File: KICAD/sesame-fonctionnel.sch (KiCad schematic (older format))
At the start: 9 parts, among them J1 CXS70-14-C, J2 CXS70-14-C, J3 6095, J4 6095, J5 6095, J6 6095, J7 CXS70-14-C, J8 CXS70-14-C

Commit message: route + work on djd
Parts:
- added H1, H2, H3, H4: MountingHole, MountingHole:MountingHole_3.2mm_M3, symbol Mechanical:MountingHole
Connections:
- net LEFT PROTECTION/IO_PWR renamed L
- net RIGHT PROTECTION/IO_PWR renamed R
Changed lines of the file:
@@
 F6 "Dir" O R 1600 5300 50
 F7 "Mode" O R 1600 5400 50
-F8 "PWM" O R 1600 4100 50
-F9 "~PWM" O R 1600 4000 50
-F10 "CC_CV_Mode" O R 1600 5500 50
-F11 "Ext_Setpoint" O R 1600 6550 50
-F12 "Ext_Current_Tresh" O R 1600 7100 50
-F13 "Ext_Voltage_Tresh" O R 1600 7000 50
-F14 "Ext_Rearm" O R 1600 6850 50
-F15 "INT_PWM_Power" I R 1600 4900 50
-F16 "~INT_PWM_Freewheel" I R 1600 4800 50
+F8 "CC_CV_Mode" O R 1600 5500 50
+F9 "Ext_Setpoint" O R 1600 6550 50
+F10 "Ext_Current_Tresh" O R 1600 7100 50
+F11 "Ext_Voltage_Tresh" O R 1600 7000 50
+F12 "Ext_Rearm" O R 1600 6850 50
+F13 "INT_PWM_Power" I R 1600 4900 50
+F14 "~INT_PWM_Freewheel" I R 1600 4800 50
+F15 "PWM_Power" O R 1600 4100 50
+F16 "~PWM_Freewheel" O R 1600 4000 50
 $EndSheet
 Wire Wire Line
@@
 F5 "PWM_Power" O R 6300 5300 50
 $EndSheet
+$Comp
+L Mechanical:MountingHole H1
+U 1 1 61346C8D
+P 10450 650
+F 0 "H1" H 10550 696 50  0000 L CNN
+F 1 "MountingHole" H 10550 605 50  0000 L CNN
+F 2 "MountingHole:MountingHole_3.2mm_M3" H 10450 650 50  0001 C CNN
+F 3 "~" H 10450 650 50  0001 C CNN
+	1    10450 650
+	1    0    0    -1
+$EndComp
+$Comp
+L Mechanical:MountingHole H2
+U 1 1 613479B3
+P 10450 850
+F 0 "H2" H 10550 896 50  0000 L CNN
+F 1 "MountingHole" H 10550 805 50  0000 L CNN
+F 2 "MountingHole:MountingHole_3.2mm_M3" H 10450 850 50  0001 C CNN
+F 3 "~" H 10450 850 50  0001 C CNN
+	1    10450 850
+	1    0    0    -1
+$EndComp
+$Comp
+L Mechanical:MountingHole H3
+U 1 1 6134C741
+P 10450 1050
+F 0 "H3" H 10550 1096 50  0000 L CNN
+F 1 "MountingHole" H 10550 1005 50  0000 L CNN
+F 2 "MountingHole:MountingHole_3.2mm_M3" H 10450 1050 50  0001 C CNN
+F 3 "~" H 10450 1050 50  0001 C CNN
+	1    10450 1050
+	1    0    0    -1
+$EndComp
+$Comp
+L Mechanical:MountingHole H4
+U 1 1 613513EA
+P 10450 1250
+F 0 "H4" H 10550 1296 50  0000 L CNN
+F 1 "MountingHole" H 10550 1205 50  0000 L CNN
+F 2 "MountingHole:MountingHole_3.2mm_M3" H 10450 1250 50  0001 C CNN
+F 3 "~" H 10450 1250 50  0001 C CNN
+	1    10450 1250
+	1    0    0    -1
+$EndComp
+Text Label 1050 2200 0    50   ~ 0
+L
+Text Label 10600 2200 0    50   ~ 0
+R
 $EndSCHEMATC

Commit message: added footprint for sepic coil + no more errors in netlist
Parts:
- removed J3, J4, J5, J6: 6095, symbol Mechanical:MountingHole_Pad
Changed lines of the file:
@@
 	1000 3250 950  3250
 $Comp
-L Mechanical:MountingHole_Pad J4
+L Mechanical:MountingHole_Pad #J4
 U 1 1 6142C008
 P 800 3100
-F 0 "J4" V 1050 3150 50  0000 C CNN
+F 0 "#J4" V 1050 3150 50  0000 C CNN
 F 1 "6095" V 950 3150 50  0000 C CNN
 F 2 "" H 800 3100 50  0001 C CNN
@@
 $EndComp
 $Comp
-L Mechanical:MountingHole_Pad J3
+L Mechanical:MountingHole_Pad #J3
 U 1 1 6142711F
 P 800 2350
-F 0 "J3" V 550 2400 50  0000 C CNN
+F 0 "#J3" V 550 2400 50  0000 C CNN
 F 1 "6095" V 650 2400 50  0000 C CNN
 F 2 "" H 800 2350 50  0001 C CNN
@@
 $EndSheet
 $Comp
-L Mechanical:MountingHole_Pad J5
+L Mechanical:MountingHole_Pad #J5
 U 1 1 61485222
 P 10900 2350
-F 0 "J5" V 10650 2400 50  0000 C CNN
+F 0 "#J5" V 10650 2400 50  0000 C CNN
 F 1 "6095" V 10750 2400 50  0000 C CNN
 F 2 "" H 10900 2350 50  0001 C CNN
@@
 	10800 3050 10700 3050
 $Comp
-L Mechanical:MountingHole_Pad J6
+L Mechanical:MountingHole_Pad #J6
 U 1 1 6156FADE
 P 10900 3050
-F 0 "J6" V 11150 3100 50  0000 C CNN
+F 0 "#J6" V 11150 3100 50  0000 C CNN
 F 1 "6095" V 11050 3100 50  0000 C CNN
 F 2 "" H 10900 3050 50  0001 C CNN

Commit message: changed monting holes + tweaks & still routing
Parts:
- H1, H2, H3, H4: footprint MountingHole:MountingHole_3.2mm_M3 -> Sesame_footprint:MountingHole_3.2mm_M3
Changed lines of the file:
@@
 F 0 "H1" H 10550 696 50  0000 L CNN
 F 1 "MountingHole" H 10550 605 50  0000 L CNN
-F 2 "MountingHole:MountingHole_3.2mm_M3" H 10450 650 50  0001 C CNN
+F 2 "Sesame_footprint:MountingHole_3.2mm_M3" H 10450 650 50  0001 C CNN
 F 3 "~" H 10450 650 50  0001 C CNN
 	1    10450 650
@@
 F 0 "H2" H 10550 896 50  0000 L CNN
 F 1 "MountingHole" H 10550 805 50  0000 L CNN
-F 2 "MountingHole:MountingHole_3.2mm_M3" H 10450 850 50  0001 C CNN
+F 2 "Sesame_footprint:MountingHole_3.2mm_M3" H 10450 850 50  0001 C CNN
 F 3 "~" H 10450 850 50  0001 C CNN
 	1    10450 850
@@
 F 0 "H3" H 10550 1096 50  0000 L CNN
 F 1 "MountingHole" H 10550 1005 50  0000 L CNN
-F 2 "MountingHole:MountingHole_3.2mm_M3" H 10450 1050 50  0001 C CNN
+F 2 "Sesame_footprint:MountingHole_3.2mm_M3" H 10450 1050 50  0001 C CNN
 F 3 "~" H 10450 1050 50  0001 C CNN
 	1    10450 1050
@@
 F 0 "H4" H 10550 1296 50  0000 L CNN
 F 1 "MountingHole" H 10550 1205 50  0000 L CNN
-F 2 "MountingHole:MountingHole_3.2mm_M3" H 10450 1250 50  0001 C CNN
+F 2 "Sesame_footprint:MountingHole_3.2mm_M3" H 10450 1250 50  0001 C CNN
 F 3 "~" H 10450 1250 50  0001 C CNN
 	1    10450 1250

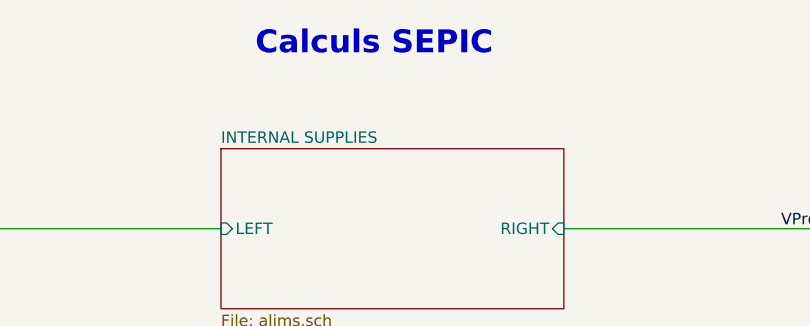
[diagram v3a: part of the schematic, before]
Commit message: mod. ref rail on kicad
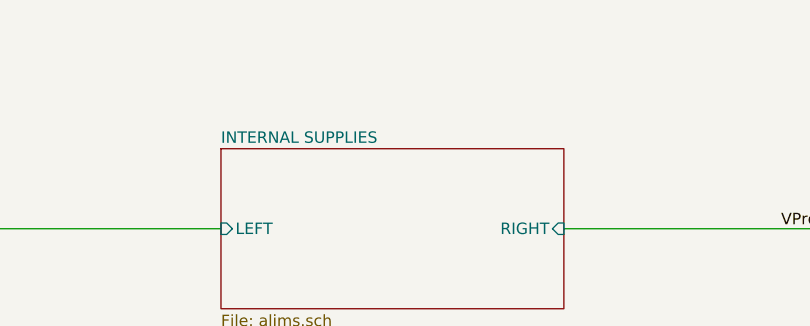
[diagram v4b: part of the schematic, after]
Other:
- note removed: "Calculs SEPIC"
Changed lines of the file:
@@
 Text Label 1950 4100 2    50   ~ 0
 PWM
-Text Notes 5200 300  0    100  ~ 20
-Calculs SEPIC
 $Sheet
 S 5050 700  1500 700

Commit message: cleanup silkscreen
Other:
- note removed: "<- VOIR PROBLEME DC"
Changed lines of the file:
@@
 Sheet 1 17
 Title "SESAME"
-Date "2021-08-17"
-Rev "0.8"
+Date "2021-08-31"
+Rev "0.9"
 Comp "ALEEA"
 Comment1 "Dessin : Guillaume Arthaud"
@@
 Voltage_Sens_L
 $Sheet
-S 3800 3200 850  550
+S 3600 3200 1050 550
 U 60F19D6C
 F0 "MOS DRIVER L" 50
 F1 "Mos_Drivers.sch" 50
 F2 "VG_P" O R 4650 3500 50
-F3 "Driver_S" I L 3800 3550 50
-F4 "Driver_P" I L 3800 3650 50
+F3 "Driver_S" I L 3600 3550 50
+F4 "Driver_P" I L 3600 3650 50
 F5 "VG_S" O R 4650 3300 50
 F6 "VS" U R 4650 3400 50
-$EndSheet
-Wire Wire Line
-	6850 2600 6850 4250
-Wire Wire Line
-	6750 4150 6750 2700
+F7 "VS_Opposite" U R 4650 3650 50
+$EndSheet
 Wire Wire Line
 	7050 1700 7050 5850
@@
 Wire Wire Line
 	2500 2200 2650 2200
-Wire Wire Line
-	4750 3300 4650 3300
-Wire Wire Line
-	4650 3400 4850 3400
-Wire Wire Line
-	4950 3500 4650 3500
-Wire Wire Line
-	6650 2800 6650 4050
-$Sheet
-S 3800 3950 850  550
+$Sheet
+S 3600 3950 1050 550
 U 619A00BB
 F0 "MOS DRIVER R" 50
 F1 "Mos_Drivers.sch" 50
-F2 "VG_P" O R 4650 4250 50
-F3 "Driver_S" I L 3800 4050 50
-F4 "Driver_P" I L 3800 4150 50
-F5 "VG_S" O R 4650 4050 50
-F6 "VS" U R 4650 4150 50
-$EndSheet
-Wire Wire Line
-	3450 3650 3800 3650
-Wire Wire Line
-	3800 3550 3450 3550
-Wire Wire Line
-	3450 4050 3800 4050
-Wire Wire Line
-	3800 4150 3450 4150
-Wire Wire Line
-	4650 4050 6650 4050
-Wire Wire Line
-	4650 4150 6750 4150
+F2 "VG_P" O R 4650 4400 50
+F3 "Driver_S" I L 3600 4050 50
+F4 "Driver_P" I L 3600 4150 50
+F5 "VG_S" O R 4650 4200 50
+F6 "VS" U R 4650 4300 50
+F7 "VS_Opposite" U R 4650 4050 50
+$EndSheet
+Wire Wire Line
+	3450 3650 3600 3650
+Wire Wire Line
+	3600 3550 3450 3550
+Wire Wire Line
+	3450 4050 3600 4050
+Wire Wire Line
+	3600 4150 3450 4150
 $Sheet
 S 5050 1950 1500 950
@@
 F9 "VS_R" U R 6550 2700 50
 $EndSheet
-Wire Wire Line
-	4650 4250 6850 4250
 $Comp
 L power:PWR_FLAG #FLG01
@@
 	1    0    0    -1
 $EndComp
-Text Notes 4800 3550 0    100  ~ 20
-<- VOIR PROBLEME DC
 $Sheet
 S 4800 5100 1500 1000
@@
 Text Label 10600 2200 0    50   ~ 0
 R
+Wire Wire Line
+	4750 3300 4650 3300
+Wire Wire Line
+	4650 3400 4850 3400
+Wire Wire Line
+	4950 3500 4650 3500
+Wire Wire Line
+	4650 4400 6850 4400
+Wire Wire Line
+	6850 2600 6850 4400
+Wire Wire Line
+	6750 4300 4650 4300
+Wire Wire Line
+	6750 2700 6750 3650
+Wire Wire Line
+	4650 4200 6650 4200
+Wire Wire Line
+	6650 2800 6650 4200
+Wire Wire Line
+	4650 3650 6750 3650
+Connection ~ 6750 3650
+Wire Wire Line
+	6750 3650 6750 4300
+Connection ~ 4850 3400
+Wire Wire Line
+	4650 4050 4850 4050
+Wire Wire Line
+	4850 4050 4850 3400
 $EndSCHEMATC

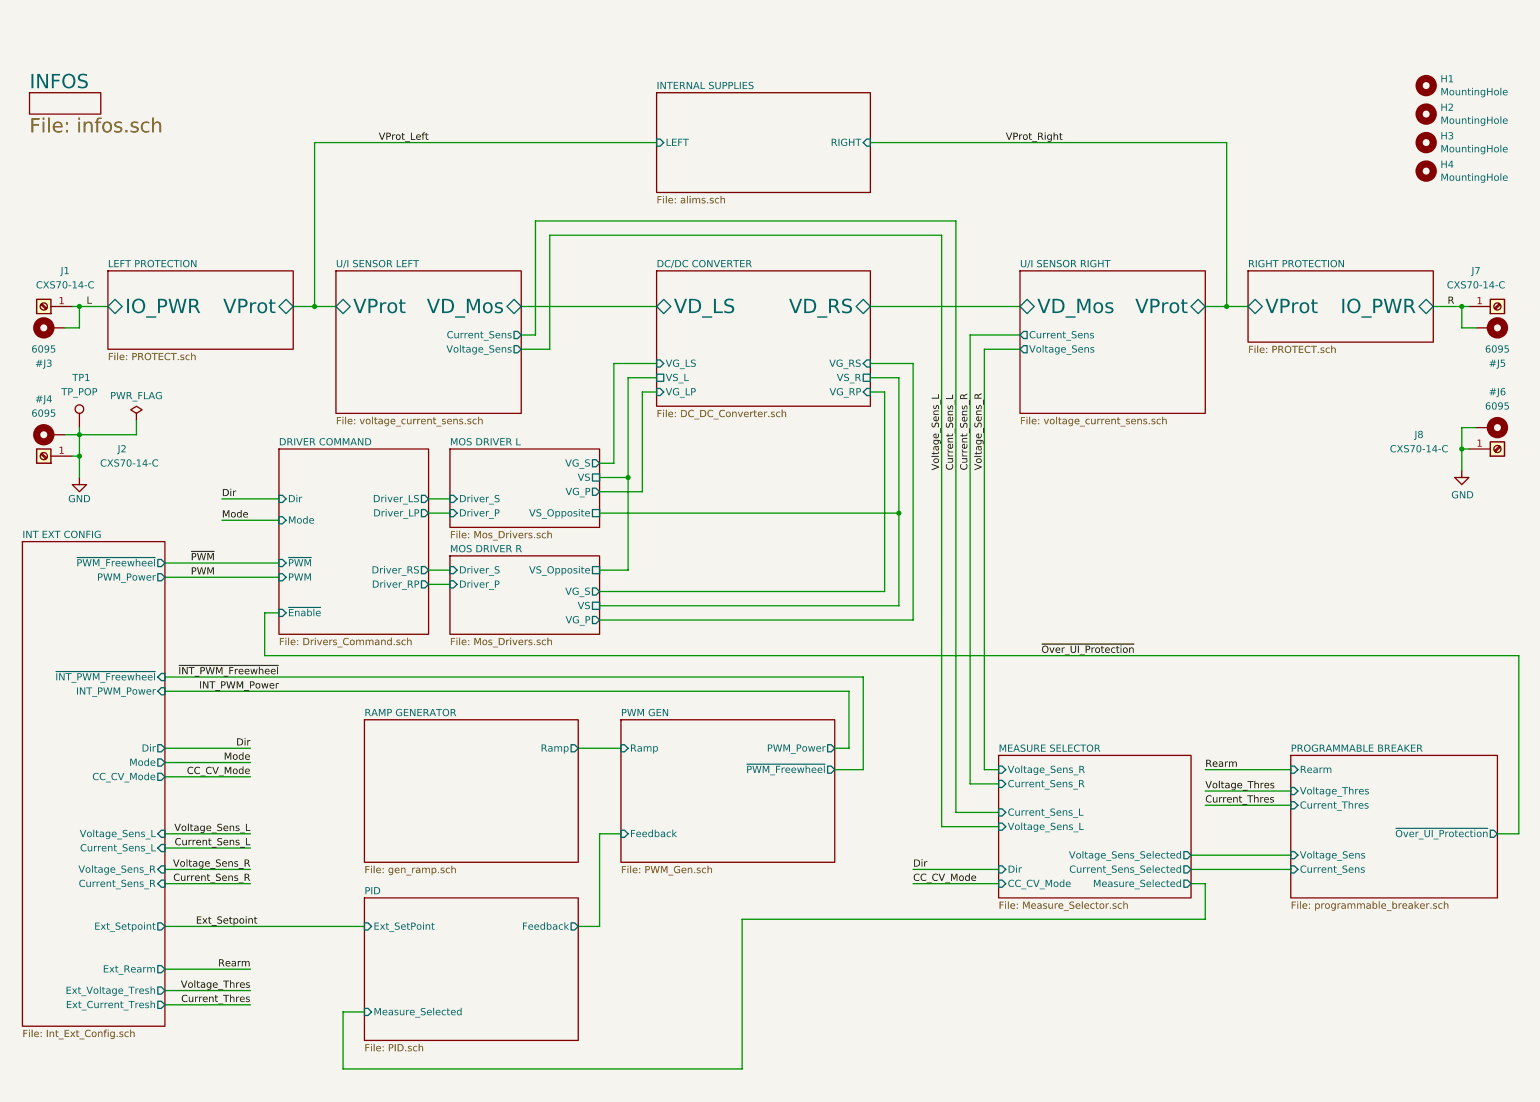
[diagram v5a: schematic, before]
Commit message: modified deadtime + added config pads on the bottom for charge pump config
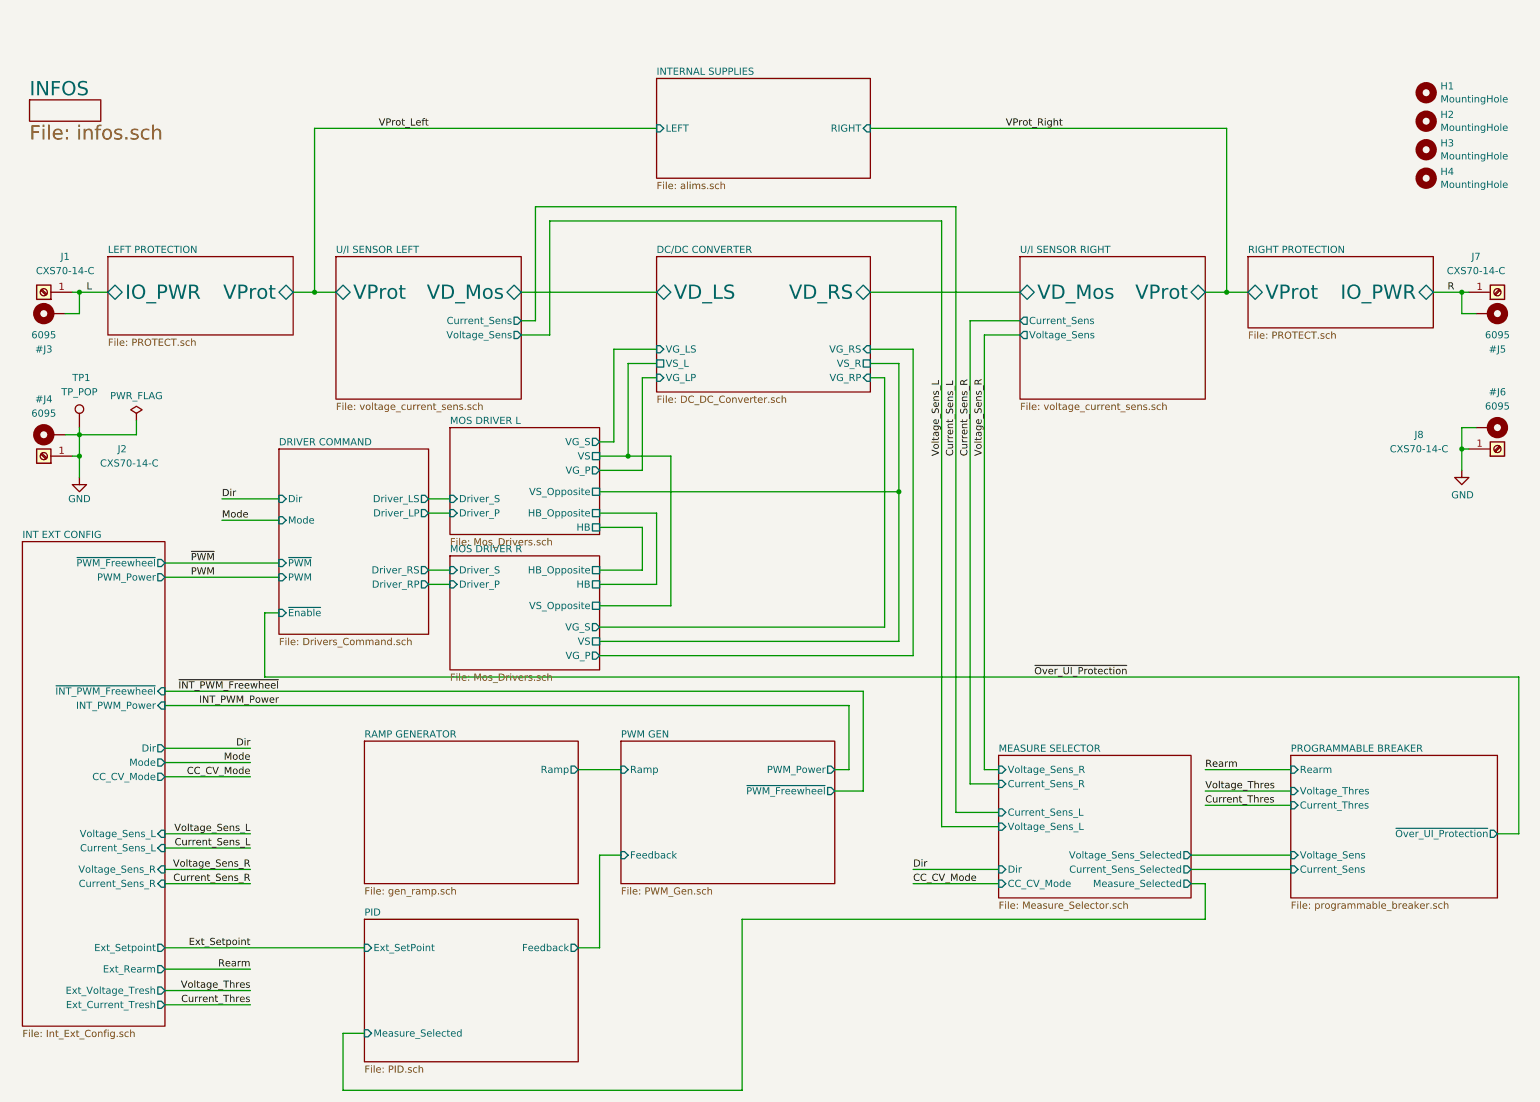
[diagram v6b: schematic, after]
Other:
- moved on the sheet: H1, H2, H3, H4, J1, J7

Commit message: lil cleanup on the main schematic sheet
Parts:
- H1, H2, H3, H4: symbol Mechanical:MountingHole -> sesame-fonctionnel-rescue:MountingHole-Mechanical
- J1, J2, J7, J8: symbol Connector:Screw_Terminal_01x01 -> sesame-fonctionnel-rescue:Screw_Terminal_01x01-Connector
- TP1: symbol Connector:TestPoint -> sesame-fonctionnel-rescue:TestPoint-Connector

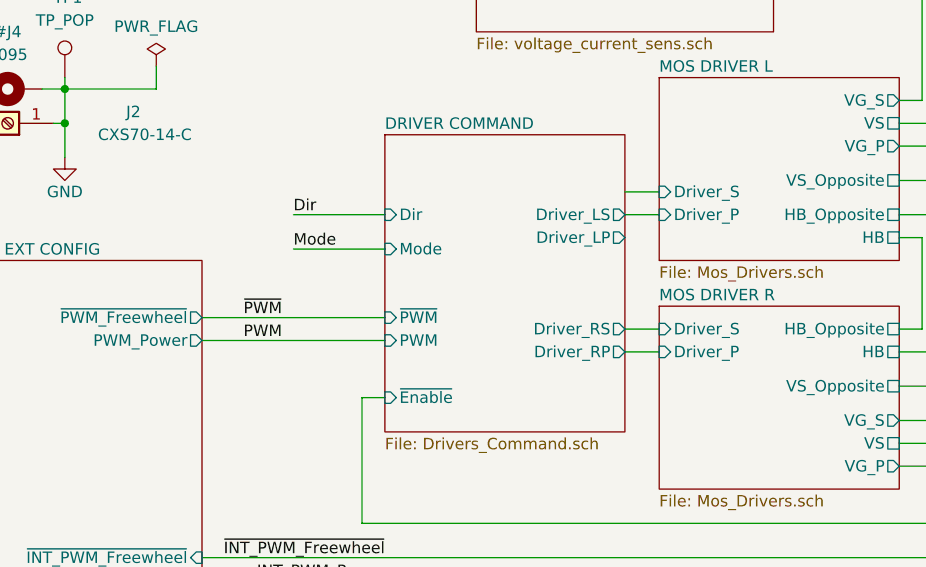
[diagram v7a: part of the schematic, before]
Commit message: fixed a mistake w/ not connected net and net naming mistake
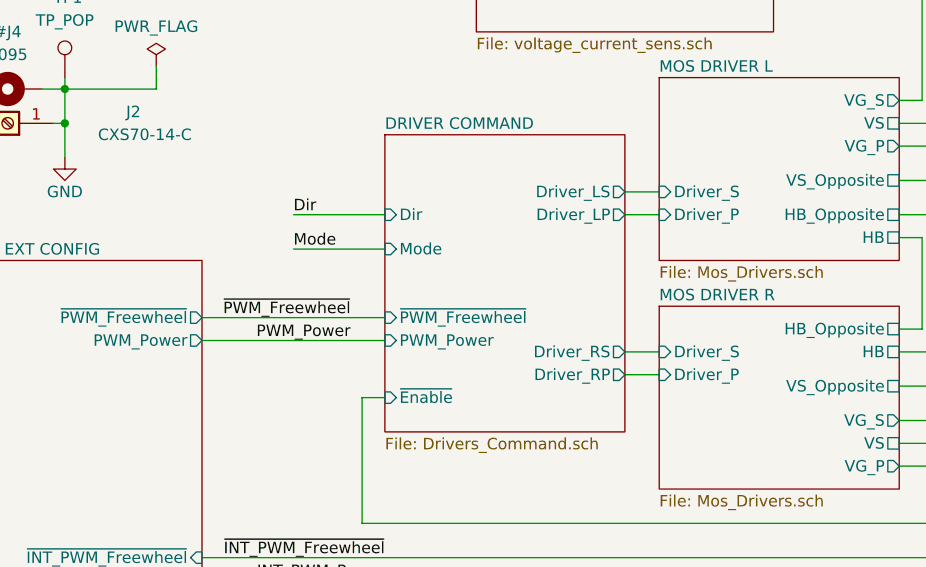
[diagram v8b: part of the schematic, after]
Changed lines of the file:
@@
 F0 "DRIVER COMMAND" 50
 F1 "Drivers_Command.sch" 50
-F2 "Driver_LS" O R 3450 3650 50
-F3 "Driver_LP" O R 3450 3750 50
-F4 "Driver_RS" O R 3450 4150 50
-F5 "Driver_RP" O R 3450 4250 50
-F6 "PWM" I L 2400 4200 50
-F7 "~PWM" I L 2400 4100 50
+F2 "Driver_LS" O R 3450 3550 50
+F3 "Driver_LP" O R 3450 3650 50
+F4 "Driver_RS" O R 3450 4250 50
+F5 "Driver_RP" O R 3450 4350 50
+F6 "PWM_Power" I L 2400 4200 50
+F7 "~PWM_Freewheel" I L 2400 4100 50
 F8 "Dir" I L 2400 3650 50
 F9 "Mode" I L 2400 3800 50
@@
 Text Label 2200 5400 2    50   ~ 0
 Dir
-Text Label 1950 4100 2    50   ~ 0
-~PWM
-Text Label 1950 4200 2    50   ~ 0
-PWM
+Text Label 2250 4100 2    50   ~ 0
+~PWM_Freewheel
+Text Label 2250 4200 2    50   ~ 0
+PWM_Power
 $Sheet
 S 5050 600  1500 700
@@
 	3450 4250 3600 4250
 Wire Wire Line
-	3600 4150 3450 4150
+	3600 4350 3450 4350
 $Sheet
 S 5050 1850 1500 950
@@
 F1 "Mos_Drivers.sch" 50
 F2 "VG_P" O R 4650 4750 50
-F3 "Driver_S" I L 3600 4150 50
-F4 "Driver_P" I L 3600 4250 50
+F3 "Driver_S" I L 3600 4250 50
+F4 "Driver_P" I L 3600 4350 50
 F5 "VG_S" O R 4650 4550 50
 F6 "VS" U R 4650 4650 50
